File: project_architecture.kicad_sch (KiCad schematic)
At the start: 0 parts

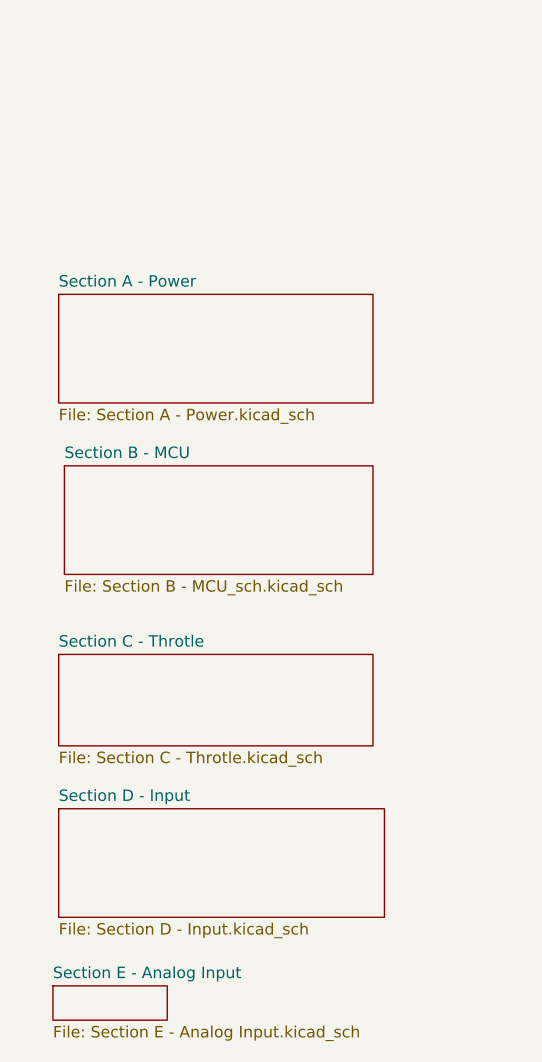
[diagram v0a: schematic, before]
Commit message: add CAN port, change power regulation
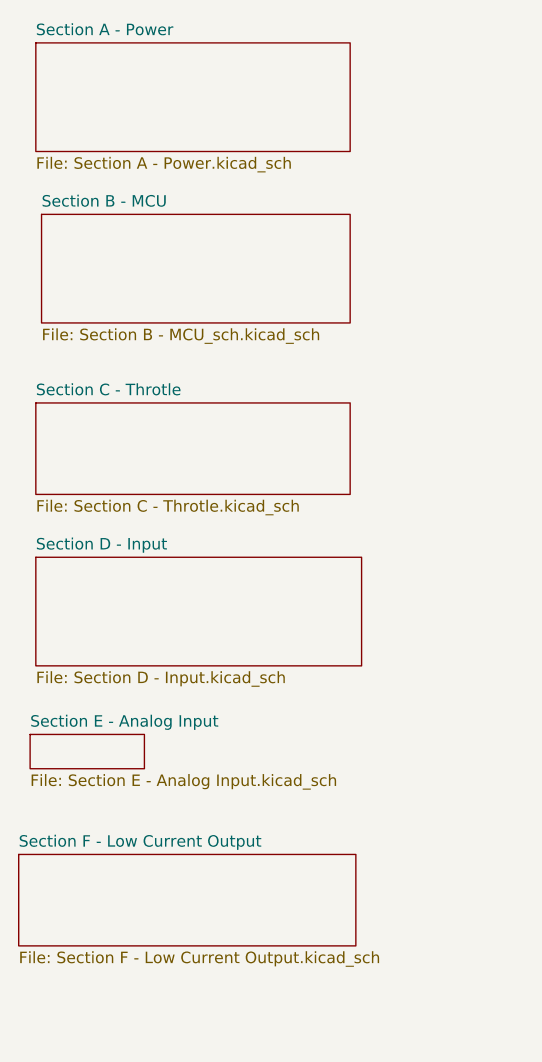
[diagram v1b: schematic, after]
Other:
- added sheet Section F - Low Current Output (Section F - Low Current Output.kicad_sch)
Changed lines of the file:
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@@
 	(paper "A4")
 	(sheet
-		(at 62.23 106.045)
+		(at 59.69 78.105)
 		(size 34.925 10.16)
 		(exclude_from_sim no)
@@
 		)
 		(property "Sheetname" "Section C - Throtle"
-			(at 62.23 105.3334 0)
+			(at 59.69 77.3934 0)
 			(show_name no)
 			(do_not_autoplace no)
@@
 		)
 		(property "Sheetfile" "Section C - Throtle.kicad_sch"
-			(at 62.23 116.7896 0)
+			(at 59.69 88.8496 0)
 			(show_name no)
 			(do_not_autoplace no)
@@
 	)
 	(sheet
-		(at 62.865 85.09)
+		(at 60.325 57.15)
 		(size 34.29 12.065)
 		(exclude_from_sim no)
@@
 		)
 		(property "Sheetname" "Section B - MCU"
-			(at 62.865 84.3784 0)
+			(at 60.325 56.4384 0)
 			(show_name no)
 			(do_not_autoplace no)
@@
 		)
 		(property "Sheetfile" "Section B - MCU_sch.kicad_sch"
-			(at 62.865 97.7396 0)
+			(at 60.325 69.7996 0)
 			(show_name no)
 			(do_not_autoplace no)
@@
 	)
 	(sheet
-		(at 62.23 66.04)
+		(at 59.69 38.1)
 		(size 34.925 12.065)
 		(exclude_from_sim no)
@@
 		)
 		(property "Sheetname" "Section A - Power"
-			(at 62.23 65.3284 0)
+			(at 59.69 37.3884 0)
 			(show_name no)
 			(do_not_autoplace no)
@@
 		)
 		(property "Sheetfile" "Section A - Power.kicad_sch"
-			(at 62.23 78.6896 0)
+			(at 59.69 50.7496 0)
 			(show_name no)
 			(do_not_autoplace no)
@@
 	)
 	(sheet
-		(at 62.23 123.19)
+		(at 57.785 128.27)
+		(size 37.465 10.16)
+		(exclude_from_sim no)
+		(in_bom yes)
+		(on_board yes)
+		(dnp no)
+		(fields_autoplaced yes)
+		(stroke
+			(width 0.1524)
+			(type solid)
+		)
+		(fill
+			(color 0 0 0 0)
+		)
+		(property "Sheetname" "Section F - Low Current Output"
+			(at 57.785 127.5584 0)
+			(show_name no)
+			(do_not_autoplace no)
+			(effects
+				(font
+					(size 1.27 1.27)
+				)
+				(justify left bottom)
+			)
+		)
+		(property "Sheetfile" "Section F - Low Current Output.kicad_sch"
+			(at 57.785 139.0146 0)
+			(show_name no)
+			(do_not_autoplace no)
+			(effects
+				(font
+					(size 1.27 1.27)
+				)
+				(justify left top)
+			)
+		)
+		(instances
+			(project "JUKEN10 Bridge"
+				(path "/ea62e1f2-9d9d-4f2f-ae78-f48dee6a9355"
+					(page "8")
+				)
+			)
+		)
+	)
+	(sheet
+		(at 59.69 95.25)
 		(size 36.195 12.065)
 		(exclude_from_sim no)
@@
 		)
 		(property "Sheetname" "Section D - Input"
-			(at 62.23 122.4784 0)
+			(at 59.69 94.5384 0)
 			(show_name no)
 			(do_not_autoplace no)
@@
 		)
 		(property "Sheetfile" "Section D - Input.kicad_sch"
-			(at 62.23 135.8396 0)
+			(at 59.69 107.8996 0)
 			(show_name no)
 			(do_not_autoplace no)
@@
 	)
 	(sheet
-		(at 61.595 142.875)
+		(at 59.055 114.935)
 		(size 12.7 3.81)
 		(exclude_from_sim no)
@@
 		)
 		(property "Sheetname" "Section E - Analog Input"
-			(at 61.595 142.1634 0)
+			(at 59.055 114.2234 0)
 			(show_name no)
 			(do_not_autoplace no)
@@
 		)
 		(property "Sheetfile" "Section E - Analog Input.kicad_sch"
-			(at 61.595 147.2696 0)
-			(show_name no)
-			(do_not_autoplace no)
+			(at 59.055 119.3296 0)
+			(show_name no)
+			(do_not_autoplace no)
